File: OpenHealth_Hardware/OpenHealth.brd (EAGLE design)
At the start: 142.2 x 125.7 mm, 22 parts

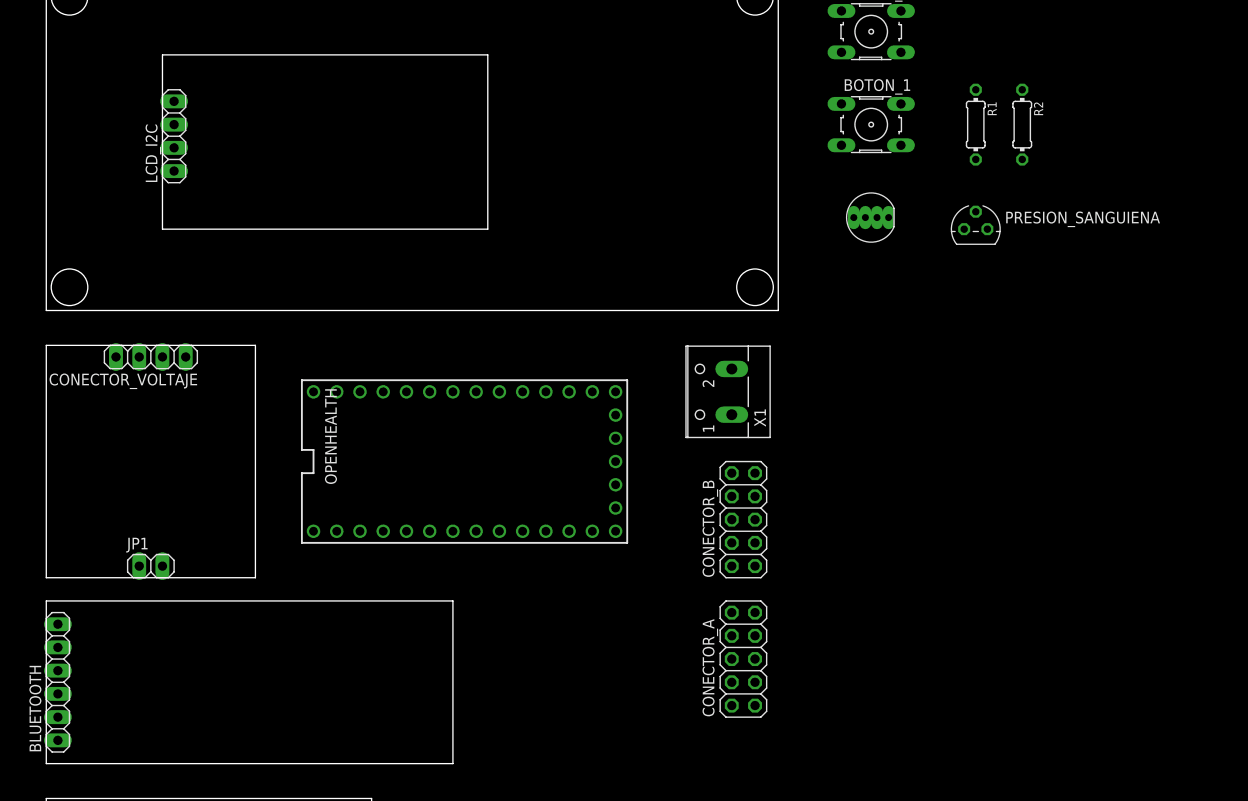
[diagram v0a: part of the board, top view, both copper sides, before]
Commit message: Creacion de los agujeros del modulo de carga
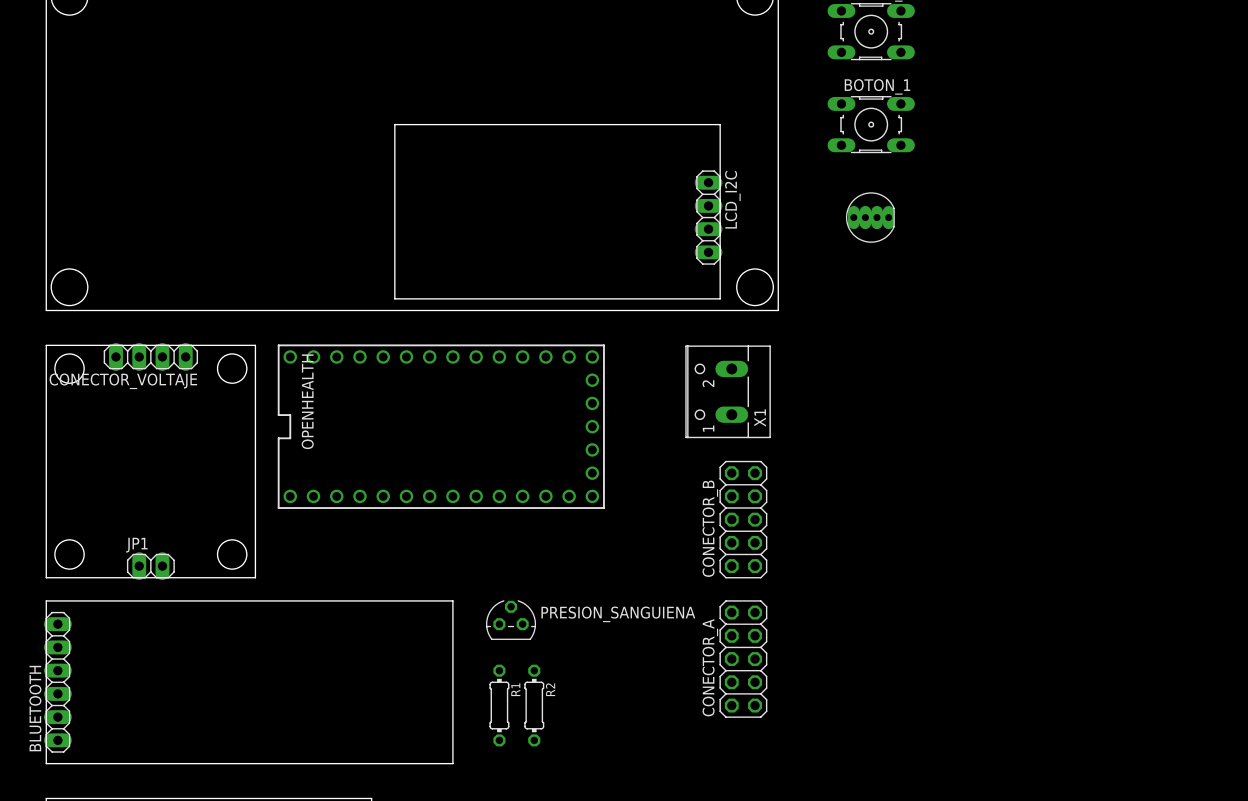
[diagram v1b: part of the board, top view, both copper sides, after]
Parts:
- moved R2 82.9 mm to (-16.5, 50.8)
- moved R1 82.1 mm to (-20.3, 50.8)
- moved PRESION_SANGUIENA 66.7 mm to (-19.1, 59.7)
- moved LCD_I2C 59.1 mm to (2.54, 104.1), turned to 270 degrees
- moved OPENHEALTH 4.58 mm to (-26.7, 81.3)
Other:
- outline, holes or cut-outs redrawn

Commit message: Creacion de espacios, se empezara a ordenar y ubicar a donde iran los componentes
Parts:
- moved OPENHEALTH 189.6 mm to (152.4, 19.1)
- moved LCA_SENSOR_PESO_A 181.6 mm to (157.5, 119.4)
- moved LCA_SENSOR_PESO_B 181.6 mm to (129.5, 119.4)
- moved BOTON_2 174.4 mm to (-152.4, 100.3)
- moved LED_RGB 155.3 mm to (-134.6, 114.3)
- moved BOTON_1 152.0 mm to (-130.8, 97.8)
- moved R1 147.9 mm to (-148.6, 124.5)
- moved PRESION_SANGUIENA 146.4 mm to (-144.8, 134.6)
- moved R2 144.6 mm to (-141.0, 124.5)
- moved CONECTOR_B 138.0 mm to (-118.1, 130.8)
- moved BLUETOOTH 126.8 mm to (-194.3, 36.8)
- moved AD8232_B 125.7 mm to (-188.0, 67.3)
- moved AD8232_A 125.7 mm to (-171.4, 53.3)
- moved U$3 125.7 mm to (-157.5, 55.9)
- moved U$4 125.7 mm to (-157.5, 76.2)
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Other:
- board size 142.2 x 125.7 mm -> 354.3 x 162.6 mm
